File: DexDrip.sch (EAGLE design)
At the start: 57 parts, among them CN2 M02JST-PTH-2, IC7 TLV71333DBV, U1 MCP73831, X1 Micro USB, Y1 48mHz Abracon

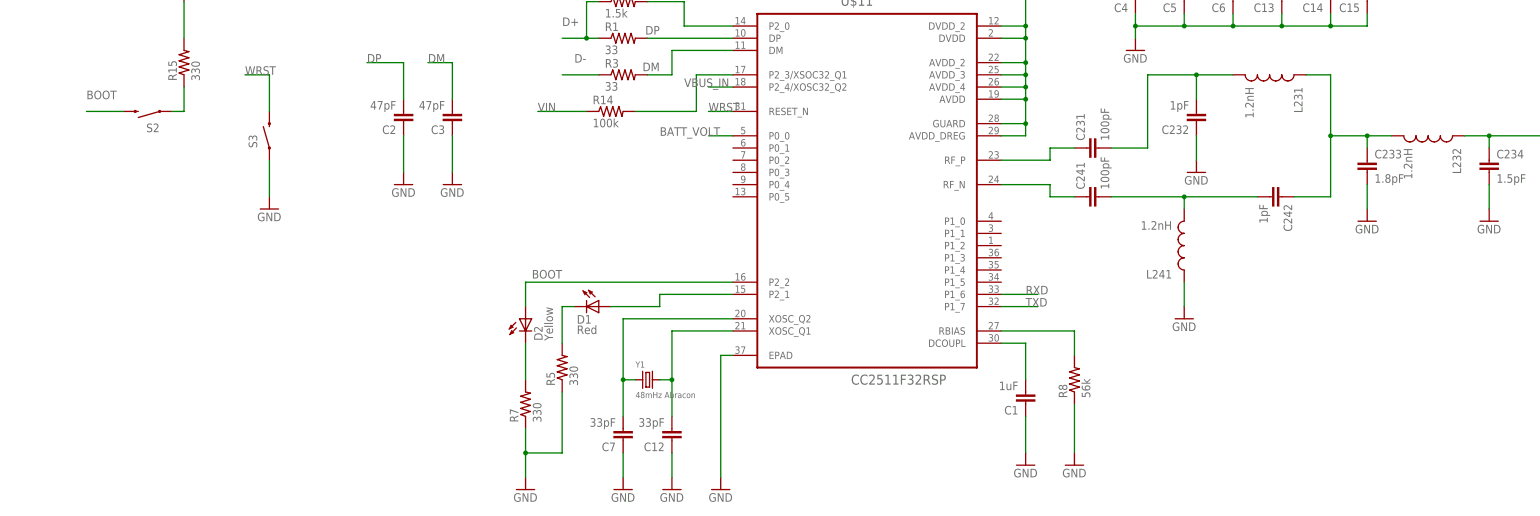
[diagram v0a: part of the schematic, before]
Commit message: Added programming pins
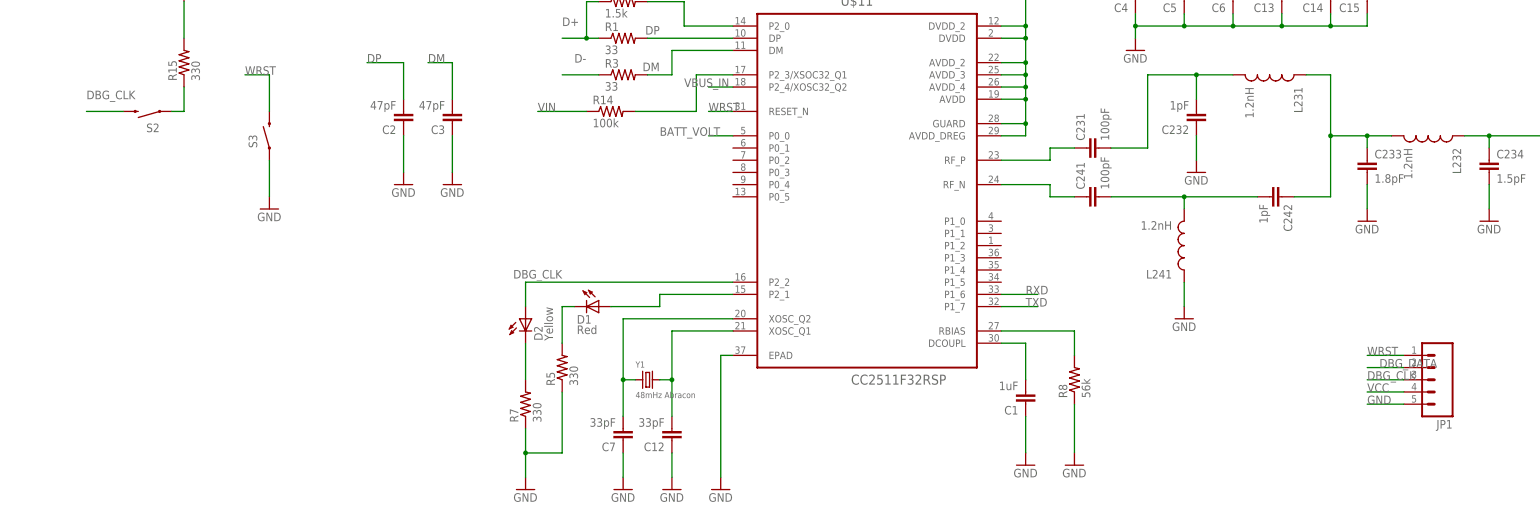
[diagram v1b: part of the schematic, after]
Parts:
- added JP1: (no value), SparkFun-Connectors:M05LOCK
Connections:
- removed net BOOT: D2.A, S2.2, U$11.P2_2
- removed net N$11: D1.A, U$11.P2_1
- new net DBG_CLK: D2.A, JP1.3, S2.2, U$11.P2_2
- new net DBG_DATA: D1.A, JP1.2, U$11.P2_1
- net GND: now also JP1.5
- net VCC: now also JP1.4
- net WRST: now also JP1.1
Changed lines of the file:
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@@
 <grid distance="0.1" unitdist="inch" unit="inch" style="lines" multiple="1" display="no" altdistance="0.01" altunitdist="inch" altunit="inch"/>
 <layers>
-<layer number="1" name="Top" color="4" fill="1" visible="no" active="no"/>
-<layer number="16" name="Bottom" color="1" fill="1" visible="no" active="no"/>
-<layer number="17" name="Pads" color="2" fill="1" visible="no" active="no"/>
-<layer number="18" name="Vias" color="2" fill="1" visible="no" active="no"/>
-<layer number="19" name="Unrouted" color="6" fill="1" visible="no" active="no"/>
-<layer number="20" name="Dimension" color="15" fill="1" visible="no" active="no"/>
-<layer number="21" name="tPlace" color="7" fill="1" visible="no" active="no"/>
-<layer number="22" name="bPlace" color="7" fill="1" visible="no" active="no"/>
-<layer number="23" name="tOrigins" color="15" fill="1" visible="no" active="no"/>
-<layer number="24" name="bOrigins" color="15" fill="1" visible="no" active="no"/>
-<layer number="25" name="tNames" color="7" fill="1" visible="no" active="no"/>
-<layer number="26" name="bNames" color="7" fill="1" visible="no" active="no"/>
-<layer number="27" name="tValues" color="7" fill="1" visible="no" active="no"/>
-<layer number="28" name="bValues" color="7" fill="1" visible="no" active="no"/>
+<layer number="1" name="Top" color="4" fill="1" visible="yes" active="no"/>
+<layer number="16" name="Bottom" color="1" fill="1" visible="yes" active="no"/>
+<layer number="17" name="Pads" color="2" fill="1" visible="yes" active="no"/>
+<layer number="18" name="Vias" color="2" fill="1" visible="yes" active="no"/>
+<layer number="19" name="Unrouted" color="6" fill="1" visible="yes" active="no"/>
+<layer number="20" name="Dimension" color="15" fill="1" visible="yes" active="no"/>
+<layer number="21" name="tPlace" color="7" fill="1" visible="yes" active="no"/>
+<layer number="22" name="bPlace" color="7" fill="1" visible="yes" active="no"/>
+<layer number="23" name="tOrigins" color="15" fill="1" visible="yes" active="no"/>
+<layer number="24" name="bOrigins" color="15" fill="1" visible="yes" active="no"/>
+<layer number="25" name="tNames" color="7" fill="1" visible="yes" active="no"/>
+<layer number="26" name="bNames" color="7" fill="1" visible="yes" active="no"/>
+<layer number="27" name="tValues" color="7" fill="1" visible="yes" active="no"/>
+<layer number="28" name="bValues" color="7" fill="1" visible="yes" active="no"/>
 <layer number="29" name="tStop" color="7" fill="3" visible="no" active="no"/>
 <layer number="30" name="bStop" color="7" fill="6" visible="no" active="no"/>
@@
 <layer number="35" name="tGlue" color="7" fill="4" visible="no" active="no"/>
 <layer number="36" name="bGlue" color="7" fill="5" visible="no" active="no"/>
-<layer number="37" name="tTest" color="7" fill="1" visible="no" active="no"/>
-<layer number="38" name="bTest" color="7" fill="1" visible="no" active="no"/>
+<layer number="37" name="tTest" color="7" fill="1" visible="yes" active="no"/>
+<layer number="38" name="bTest" color="7" fill="1" visible="yes" active="no"/>
 <layer number="39" name="tKeepout" color="4" fill="11" visible="no" active="no"/>
 <layer number="40" name="bKeepout" color="1" fill="11" visible="no" active="no"/>
@@
 <layer number="44" name="Drills" color="7" fill="1" visible="no" active="no"/>
 <layer number="45" name="Holes" color="7" fill="1" visible="no" active="no"/>
-<layer number="46" name="Milling" color="3" fill="1" visible="no" active="no"/>
-<layer number="47" name="Measures" color="7" fill="1" visible="no" active="no"/>
-<layer number="48" name="Document" color="7" fill="1" visible="no" active="no"/>
-<layer number="49" name="Reference" color="7" fill="1" visible="no" active="no"/>
-<layer number="50" name="dxf" color="7" fill="1" visible="no" active="no"/>
-<layer number="51" name="tDocu" color="7" fill="1" visible="no" active="no"/>
-<layer number="52" name="bDocu" color="7" fill="1" visible="no" active="no"/>
-<layer number="53" name="tGND_GNDA" color="7" fill="9" visible="no" active="no"/>
-<layer number="54" name="bGND_GNDA" color="1" fill="9" visible="no" active="no"/>
-<layer number="56" name="wert" color="7" fill="1" visible="no" active="no"/>
-<layer number="57" name="tCAD" color="7" fill="1" visible="no" active="no"/>
+<layer number="46" name="Milling" color="3" fill="1" visible="yes" active="no"/>
+<layer number="47" name="Measures" color="7" fill="1" visible="yes" active="no"/>
+<layer number="48" name="Document" color="7" fill="1" visible="yes" active="no"/>
+<layer number="49" name="Reference" color="7" fill="1" visible="yes" active="no"/>
+<layer number="50" name="dxf" color="7" fill="1" visible="yes" active="no"/>
+<layer number="51" name="tDocu" color="7" fill="1" visible="yes" active="no"/>
+<layer number="52" name="bDocu" color="7" fill="1" visible="yes" active="no"/>
+<layer number="53" name="tGND_GNDA" color="7" fill="9" visible="yes" active="no"/>
+<layer number="54" name="bGND_GNDA" color="1" fill="9" visible="yes" active="no"/>
+<layer number="56" name="wert" color="7" fill="1" visible="yes" active="no"/>
+<layer number="57" name="tCAD" color="7" fill="1" visible="yes" active="no"/>
 <layer number="90" name="Modules" color="5" fill="1" visible="yes" active="yes"/>
 <layer number="91" name="Nets" color="2" fill="1" visible="yes" active="yes"/>
@@
 <part name="LOGO1" library="IdleHandsProject" deviceset="IDLEHANDS_LOGO" device="S"/>
 <part name="LOGO2" library="SparkFun-Aesthetics" deviceset="OSHW-LOGO" device="S"/>
+<part name="JP1" library="SparkFun-Connectors" deviceset="M05" device="LOCK"/>
 </parts>
 <sheets>
@@
 <instance part="LOGO1" gate="G$1" x="-132.08" y="223.52"/>
 <instance part="LOGO2" gate="G$1" x="-86.36" y="220.98"/>
+<instance part="JP1" gate="G$1" x="162.56" y="10.16" rot="R180"/>
 </instances>
 <busses>
@@
 <wire x1="-81.28" y1="55.88" x2="-81.28" y2="48.26" width="0.1524" layer="91"/>
 <pinref part="GND22" gate="1" pin="GND"/>
+</segment>
+<segment>
+<pinref part="JP1" gate="G$1" pin="5"/>
+<wire x1="154.94" y1="5.08" x2="147.32" y2="5.08" width="0.1524" layer="91"/>
+<label x="147.32" y="5.08" size="1.778" layer="95"/>
 </segment>
 </net>
@@
 <pinref part="P+4" gate="1" pin="VCC"/>
 </segment>
+<segment>
+<pinref part="JP1" gate="G$1" pin="4"/>
+<wire x1="154.94" y1="7.62" x2="147.32" y2="7.62" width="0.1524" layer="91"/>
+<label x="147.32" y="7.62" size="1.778" layer="95"/>
+</segment>
 </net>
 <net name="N$6" class="0">
@@
 </segment>
 </net>
-<net name="BOOT" class="0">
-<segment>
-<pinref part="U$11" gate="G$1" pin="P2_2"/>
-<wire x1="15.24" y1="30.48" x2="-27.94" y2="30.48" width="0.1524" layer="91"/>
-<wire x1="-27.94" y1="30.48" x2="-27.94" y2="25.4" width="0.1524" layer="91"/>
-<pinref part="D2" gate="G$1" pin="A"/>
-<label x="-20.32" y="33.02" size="1.778" layer="95" rot="R180"/>
-</segment>
-<segment>
-<pinref part="S2" gate="G$1" pin="2"/>
-<wire x1="-111.76" y1="66.04" x2="-119.38" y2="66.04" width="0.1524" layer="91"/>
-<label x="-119.38" y="68.58" size="1.778" layer="95"/>
-</segment>
-</net>
-<net name="N$11" class="0">
-<segment>
-<pinref part="U$11" gate="G$1" pin="P2_1"/>
-<wire x1="15.24" y1="27.94" x2="0" y2="27.94" width="0.1524" layer="91"/>
-<wire x1="0" y1="27.94" x2="0" y2="25.4" width="0.1524" layer="91"/>
-<wire x1="0" y1="25.4" x2="-10.16" y2="25.4" width="0.1524" layer="91"/>
-<pinref part="D1" gate="G$1" pin="A"/>
-</segment>
-</net>
 <net name="N$12" class="0">
 <segment>
@@
 <pinref part="S3" gate="G$1" pin="2"/>
 </segment>
+<segment>
+<pinref part="JP1" gate="G$1" pin="1"/>
+<wire x1="154.94" y1="15.24" x2="147.32" y2="15.24" width="0.1524" layer="91"/>
+<label x="147.32" y="15.24" size="1.778" layer="95"/>
+</segment>
 </net>
 <net name="N$8" class="0">
@@
 </segment>
 </net>
+<net name="DBG_CLK" class="0">
+<segment>
+<pinref part="JP1" gate="G$1" pin="3"/>
+<wire x1="154.94" y1="10.16" x2="147.32" y2="10.16" width="0.1524" layer="91"/>
+<label x="147.32" y="10.16" size="1.778" layer="95"/>
+</segment>
+<segment>
+<pinref part="U$11" gate="G$1" pin="P2_2"/>
+<wire x1="15.24" y1="30.48" x2="-27.94" y2="30.48" width="0.1524" layer="91"/>
+<wire x1="-27.94" y1="30.48" x2="-27.94" y2="25.4" width="0.1524" layer="91"/>
+<pinref part="D2" gate="G$1" pin="A"/>
+<label x="-20.32" y="33.02" size="1.778" layer="95" rot="R180"/>
+</segment>
+<segment>
+<pinref part="S2" gate="G$1" pin="2"/>
+<wire x1="-111.76" y1="66.04" x2="-119.38" y2="66.04" width="0.1524" layer="91"/>
+<label x="-119.38" y="68.58" size="1.778" layer="95"/>
+</segment>
+</net>
+<net name="DBG_DATA" class="0">
+<segment>
+<pinref part="JP1" gate="G$1" pin="2"/>
+<wire x1="154.94" y1="12.7" x2="147.32" y2="12.7" width="0.1524" layer="91"/>
+<label x="149.86" y="12.7" size="1.778" layer="95"/>
+</segment>
+<segment>
+<pinref part="U$11" gate="G$1" pin="P2_1"/>
+<wire x1="15.24" y1="27.94" x2="0" y2="27.94" width="0.1524" layer="91"/>
+<wire x1="0" y1="27.94" x2="0" y2="25.4" width="0.1524" layer="91"/>
+<wire x1="0" y1="25.4" x2="-10.16" y2="25.4" width="0.1524" layer="91"/>
+<pinref part="D1" gate="G$1" pin="A"/>
+</segment>
+</net>

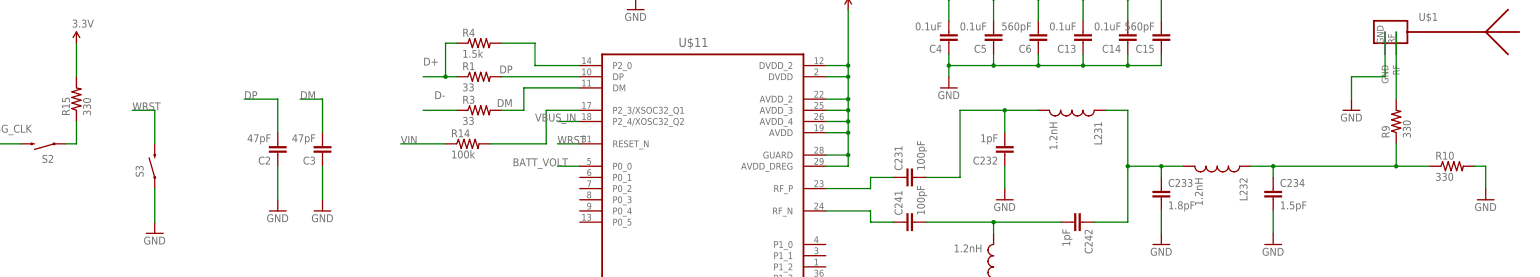
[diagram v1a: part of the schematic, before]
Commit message: Fixes some R Values RF WORKING
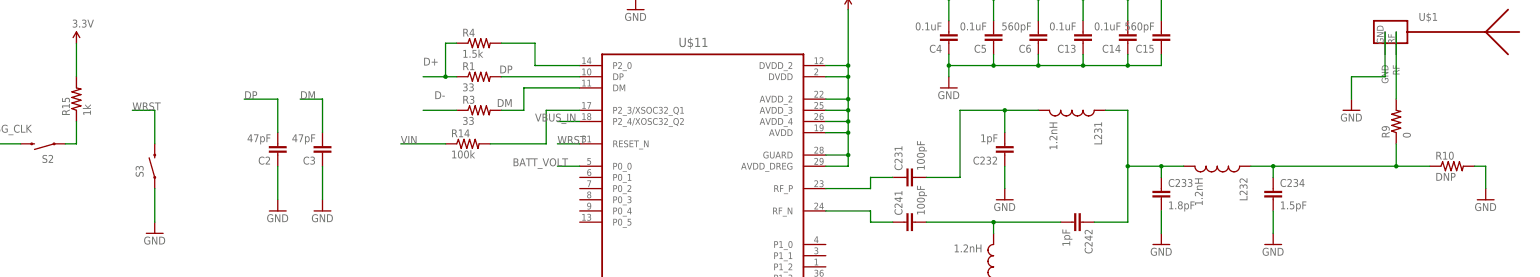
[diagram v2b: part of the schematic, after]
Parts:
- R10: value 330 -> DNP
- R15: value 330 -> 1k
- R9: value 330 -> 0
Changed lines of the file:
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@@
 <?xml version="1.0" encoding="utf-8"?>
 <!DOCTYPE eagle SYSTEM "eagle.dtd">
-<eagle version="7.1.0">
+<eagle version="7.2.0">
 <drawing>
 <settings>
@@
 <grid distance="0.1" unitdist="inch" unit="inch" style="lines" multiple="1" display="no" altdistance="0.01" altunitdist="inch" altunit="inch"/>
 <layers>
-<layer number="1" name="Top" color="4" fill="1" visible="yes" active="no"/>
-<layer number="16" name="Bottom" color="1" fill="1" visible="yes" active="no"/>
-<layer number="17" name="Pads" color="2" fill="1" visible="yes" active="no"/>
-<layer number="18" name="Vias" color="2" fill="1" visible="yes" active="no"/>
-<layer number="19" name="Unrouted" color="6" fill="1" visible="yes" active="no"/>
-<layer number="20" name="Dimension" color="15" fill="1" visible="yes" active="no"/>
-<layer number="21" name="tPlace" color="7" fill="1" visible="yes" active="no"/>
-<layer number="22" name="bPlace" color="7" fill="1" visible="yes" active="no"/>
-<layer number="23" name="tOrigins" color="15" fill="1" visible="yes" active="no"/>
-<layer number="24" name="bOrigins" color="15" fill="1" visible="yes" active="no"/>
-<layer number="25" name="tNames" color="7" fill="1" visible="yes" active="no"/>
-<layer number="26" name="bNames" color="7" fill="1" visible="yes" active="no"/>
-<layer number="27" name="tValues" color="7" fill="1" visible="yes" active="no"/>
-<layer number="28" name="bValues" color="7" fill="1" visible="yes" active="no"/>
+<layer number="1" name="Top" color="4" fill="1" visible="no" active="no"/>
+<layer number="16" name="Bottom" color="1" fill="1" visible="no" active="no"/>
+<layer number="17" name="Pads" color="2" fill="1" visible="no" active="no"/>
+<layer number="18" name="Vias" color="2" fill="1" visible="no" active="no"/>
+<layer number="19" name="Unrouted" color="6" fill="1" visible="no" active="no"/>
+<layer number="20" name="Dimension" color="15" fill="1" visible="no" active="no"/>
+<layer number="21" name="tPlace" color="7" fill="1" visible="no" active="no"/>
+<layer number="22" name="bPlace" color="7" fill="1" visible="no" active="no"/>
+<layer number="23" name="tOrigins" color="15" fill="1" visible="no" active="no"/>
+<layer number="24" name="bOrigins" color="15" fill="1" visible="no" active="no"/>
+<layer number="25" name="tNames" color="7" fill="1" visible="no" active="no"/>
+<layer number="26" name="bNames" color="7" fill="1" visible="no" active="no"/>
+<layer number="27" name="tValues" color="7" fill="1" visible="no" active="no"/>
+<layer number="28" name="bValues" color="7" fill="1" visible="no" active="no"/>
 <layer number="29" name="tStop" color="7" fill="3" visible="no" active="no"/>
 <layer number="30" name="bStop" color="7" fill="6" visible="no" active="no"/>
@@
 <layer number="35" name="tGlue" color="7" fill="4" visible="no" active="no"/>
 <layer number="36" name="bGlue" color="7" fill="5" visible="no" active="no"/>
-<layer number="37" name="tTest" color="7" fill="1" visible="yes" active="no"/>
-<layer number="38" name="bTest" color="7" fill="1" visible="yes" active="no"/>
+<layer number="37" name="tTest" color="7" fill="1" visible="no" active="no"/>
+<layer number="38" name="bTest" color="7" fill="1" visible="no" active="no"/>
 <layer number="39" name="tKeepout" color="4" fill="11" visible="no" active="no"/>
 <layer number="40" name="bKeepout" color="1" fill="11" visible="no" active="no"/>
@@
 <layer number="44" name="Drills" color="7" fill="1" visible="no" active="no"/>
 <layer number="45" name="Holes" color="7" fill="1" visible="no" active="no"/>
-<layer number="46" name="Milling" color="3" fill="1" visible="yes" active="no"/>
-<layer number="47" name="Measures" color="7" fill="1" visible="yes" active="no"/>
-<layer number="48" name="Document" color="7" fill="1" visible="yes" active="no"/>
-<layer number="49" name="Reference" color="7" fill="1" visible="yes" active="no"/>
-<layer number="50" name="dxf" color="7" fill="1" visible="yes" active="no"/>
-<layer number="51" name="tDocu" color="7" fill="1" visible="yes" active="no"/>
-<layer number="52" name="bDocu" color="7" fill="1" visible="yes" active="no"/>
-<layer number="53" name="tGND_GNDA" color="7" fill="9" visible="yes" active="no"/>
-<layer number="54" name="bGND_GNDA" color="1" fill="9" visible="yes" active="no"/>
-<layer number="56" name="wert" color="7" fill="1" visible="yes" active="no"/>
-<layer number="57" name="tCAD" color="7" fill="1" visible="yes" active="no"/>
+<layer number="46" name="Milling" color="3" fill="1" visible="no" active="no"/>
+<layer number="47" name="Measures" color="7" fill="1" visible="no" active="no"/>
+<layer number="48" name="Document" color="7" fill="1" visible="no" active="no"/>
+<layer number="49" name="Reference" color="7" fill="1" visible="no" active="no"/>
+<layer number="50" name="dxf" color="7" fill="1" visible="no" active="no"/>
+<layer number="51" name="tDocu" color="7" fill="1" visible="no" active="no"/>
+<layer number="52" name="bDocu" color="7" fill="1" visible="no" active="no"/>
+<layer number="53" name="tGND_GNDA" color="7" fill="9" visible="no" active="no"/>
+<layer number="54" name="bGND_GNDA" color="1" fill="9" visible="no" active="no"/>
+<layer number="56" name="wert" color="7" fill="1" visible="no" active="no"/>
+<layer number="57" name="tCAD" color="7" fill="1" visible="no" active="no"/>
 <layer number="90" name="Modules" color="5" fill="1" visible="yes" active="yes"/>
 <layer number="91" name="Nets" color="2" fill="1" visible="yes" active="yes"/>
@@
 <part name="L231" library="SparkFun-Passives" deviceset="INDUCTOR" device="0402" value="1.2nH"/>
 <part name="L232" library="SparkFun-Passives" deviceset="INDUCTOR" device="0402" value="1.2nH"/>
-<part name="R10" library="SparkFun" deviceset="RESISTOR" device="0402-RES" value="330"/>
-<part name="R9" library="SparkFun" deviceset="RESISTOR" device="0402-RES" value="330"/>
+<part name="R10" library="SparkFun" deviceset="RESISTOR" device="0402-RES" value="DNP"/>
+<part name="R9" library="SparkFun" deviceset="RESISTOR" device="0402-RES" value="0"/>
 <part name="GND3" library="SparkFun-Aesthetics" deviceset="GND" device=""/>
 <part name="GND4" library="SparkFun-Aesthetics" deviceset="GND" device=""/>
@@
 <part name="R14" library="SparkFun" deviceset="RESISTOR" device="0402-RES" value="100k"/>
 <part name="GND22" library="SparkFun-Aesthetics" deviceset="GND" device=""/>
-<part name="R15" library="SparkFun" deviceset="RESISTOR" device="0402-RES" value="330"/>
+<part name="R15" library="SparkFun" deviceset="RESISTOR" device="0402-RES" value="1k"/>
 <part name="P+4" library="SparkFun" deviceset="VCC" device="" value="3.3V"/>
 <part name="LOGO1" library="IdleHandsProject" deviceset="IDLEHANDS_LOGO" device="S"/>
